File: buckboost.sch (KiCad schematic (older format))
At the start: 20 parts, among them SW1 SPST, U1 TPS63060

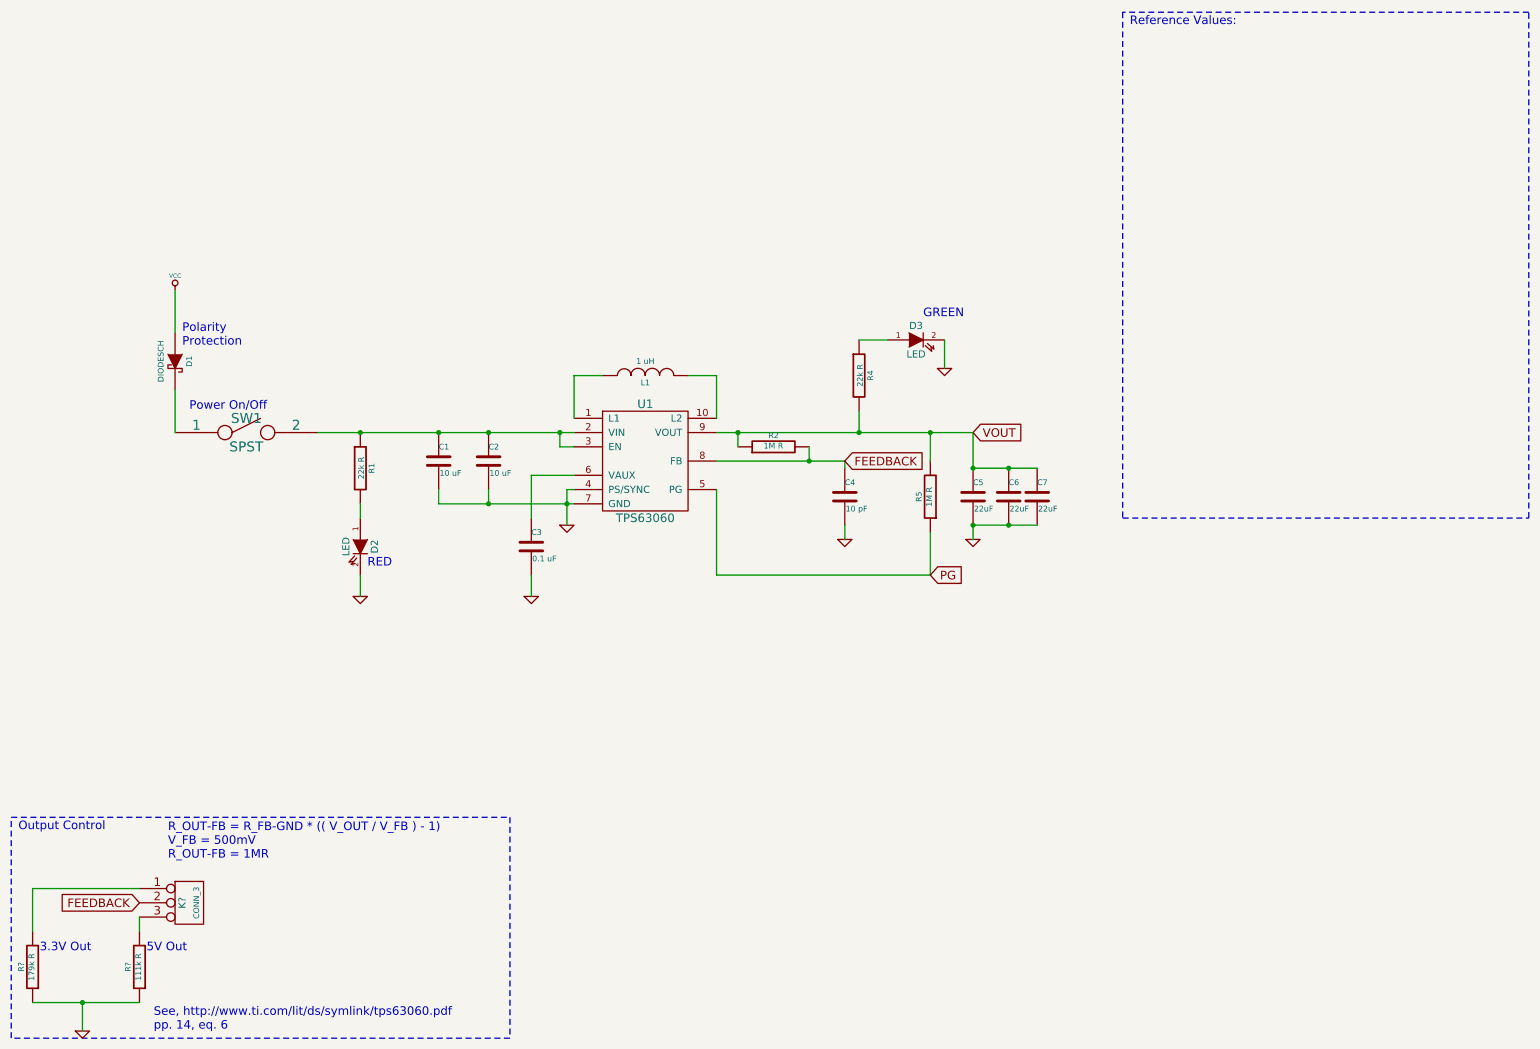
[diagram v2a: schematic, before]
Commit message: Added reference value chart from TI datasheet.
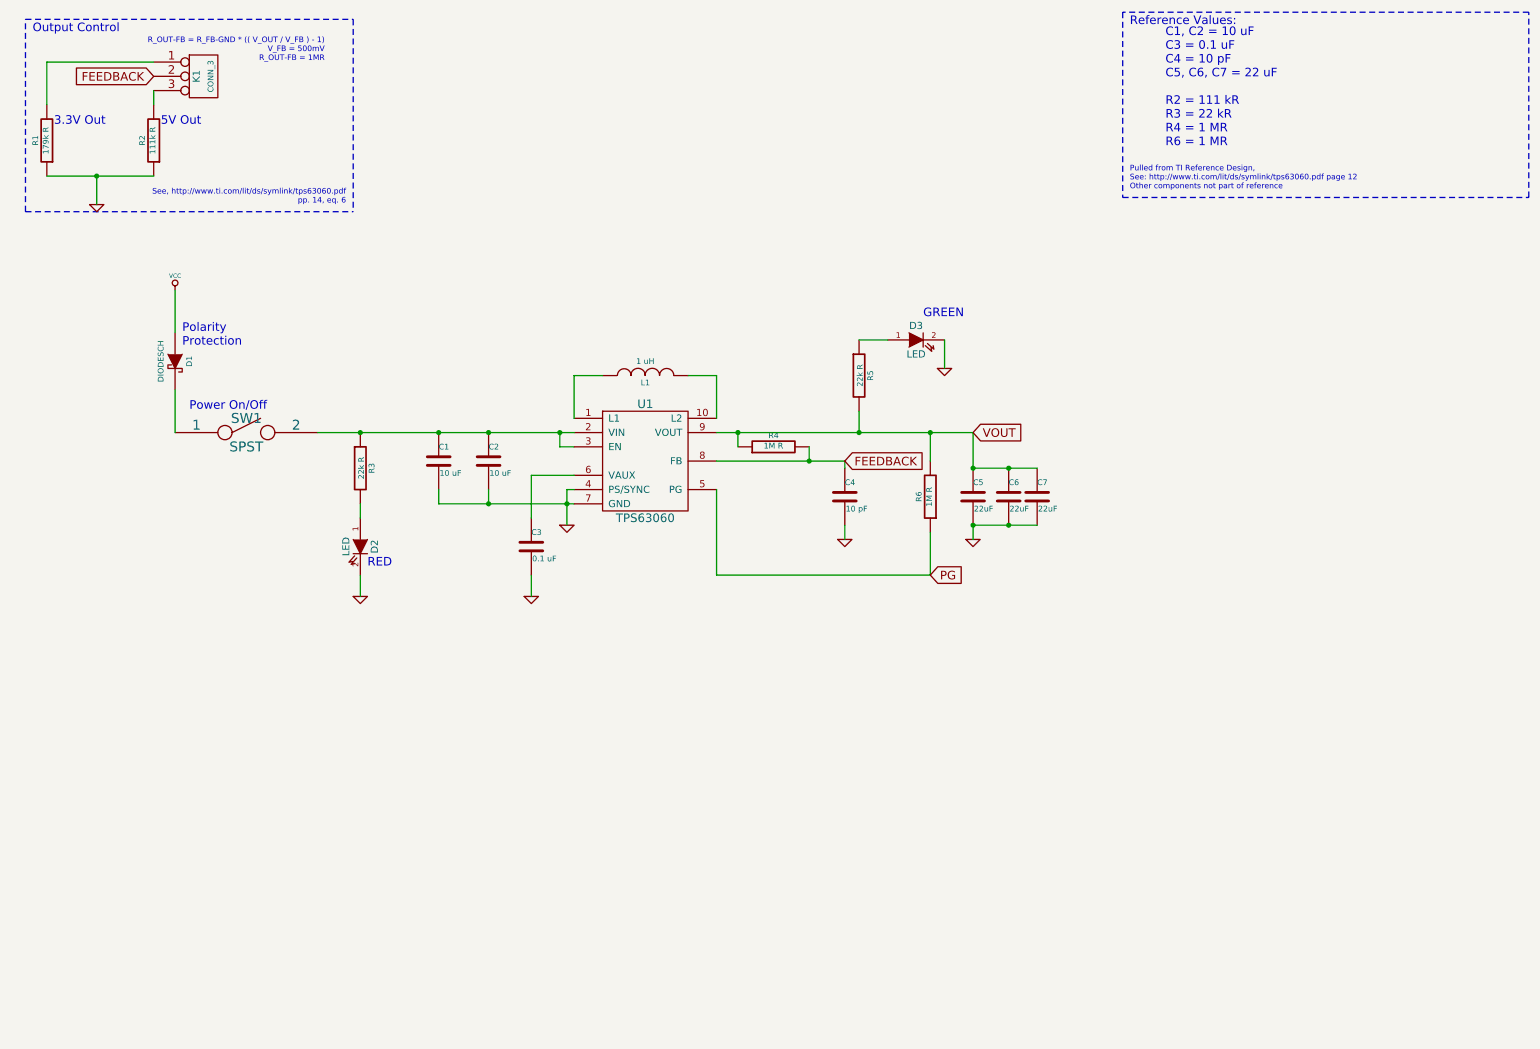
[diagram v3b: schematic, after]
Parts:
- gave numbers to parts that had none: 3
- renumbered R1 to R3, R2 to R4, R4 to R5, R5 to R6
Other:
- note added: "C1, C2 = 10 uF\nC3 = 0.1 uF\nC4 = 10 pF\nC5, C6, C7 = 22 uF\n\nR2 = 111 kR\nR3 = 22 kR\nR4 = 1 MR\nR6 = 1 MR\n"
- note added: "Pulled from TI Reference Design,\nSee: http://www.ti.com/lit/ds/symlink/tps63060.pdf page 12\nOther components not part of reference"
- moved on the sheet: K1, R1, R2
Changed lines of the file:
@@
 $EndComp
 $Comp
-L GND #PWR4
+L GND #PWR5
 U 1 1 56ED0689
 P 4400 4150
-F 0 "#PWR4" H 4400 4150 30  0001 C CNN
+F 0 "#PWR5" H 4400 4150 30  0001 C CNN
 F 1 "GND" H 4400 4080 30  0001 C CNN
 F 2 "" H 4400 4150 60  0000 C CNN
@@
 $EndComp
 $Comp
-L VCC #PWR1
+L VCC #PWR2
 U 1 1 56ED06A7
 P 1650 2500
-F 0 "#PWR1" H 1650 2600 30  0001 C CNN
+F 0 "#PWR2" H 1650 2600 30  0001 C CNN
 F 1 "VCC" H 1650 2600 30  0000 C CNN
 F 2 "" H 1650 2500 60  0000 C CNN
@@
 $EndComp
 $Comp
-L GND #PWR3
+L GND #PWR4
 U 1 1 56ED0918
 P 4150 4650
-F 0 "#PWR3" H 4150 4650 30  0001 C CNN
+F 0 "#PWR4" H 4150 4650 30  0001 C CNN
 F 1 "GND" H 4150 4580 30  0001 C CNN
 F 2 "" H 4150 4650 60  0000 C CNN
@@
 $EndComp
 $Comp
-L R R2
+L R R4
 U 1 1 56ED0C06
 P 5850 3600
-F 0 "R2" V 5930 3600 40  0000 C CNN
+F 0 "R4" V 5930 3600 40  0000 C CNN
 F 1 "1M R" V 5857 3601 40  0000 C CNN
 F 2 "" V 5780 3600 30  0000 C CNN
@@
 $EndComp
 $Comp
-L GND #PWR5
+L GND #PWR6
 U 1 1 56ED0DD5
 P 6350 4250
-F 0 "#PWR5" H 6350 4250 30  0001 C CNN
+F 0 "#PWR6" H 6350 4250 30  0001 C CNN
 F 1 "GND" H 6350 4180 30  0001 C CNN
 F 2 "" H 6350 4250 60  0000 C CNN
@@
 $EndComp
 $Comp
-L R R5
+L R R6
 U 1 1 56ED0E93
 P 6950 3950
-F 0 "R5" V 7030 3950 40  0000 C CNN
+F 0 "R6" V 7030 3950 40  0000 C CNN
 F 1 "1M R" V 6957 3951 40  0000 C CNN
 F 2 "" V 6880 3950 30  0000 C CNN
@@
 $EndComp
 $Comp
-L GND #PWR7
+L GND #PWR8
 U 1 1 56ED0F95
 P 7250 4250
-F 0 "#PWR7" H 7250 4250 30  0001 C CNN
+F 0 "#PWR8" H 7250 4250 30  0001 C CNN
 F 1 "GND" H 7250 4180 30  0001 C CNN
 F 2 "" H 7250 4250 60  0000 C CNN
@@
 Power On/Off
 $Comp
-L R R4
+L R R5
 U 1 1 56EE6E39
 P 6450 3100
-F 0 "R4" V 6530 3100 40  0000 C CNN
+F 0 "R5" V 6530 3100 40  0000 C CNN
 F 1 "22k R" V 6457 3101 40  0000 C CNN
 F 2 "" V 6380 3100 30  0000 C CNN
@@
 $EndComp
 $Comp
-L GND #PWR6
+L GND #PWR7
 U 1 1 56EE6F42
 P 7050 3050
-F 0 "#PWR6" H 7050 3050 30  0001 C CNN
+F 0 "#PWR7" H 7050 3050 30  0001 C CNN
 F 1 "GND" H 7050 2980 30  0001 C CNN
 F 2 "" H 7050 3050 60  0000 C CNN
@@
 $EndComp
 $Comp
-L R R1
+L R R3
 U 1 1 56EF9A6F
 P 2950 3750
-F 0 "R1" V 3030 3750 40  0000 C CNN
+F 0 "R3" V 3030 3750 40  0000 C CNN
 F 1 "22k R" V 2957 3751 40  0000 C CNN
 F 2 "" V 2880 3750 30  0000 C CNN
@@
 $EndComp
 $Comp
-L GND #PWR2
+L GND #PWR3
 U 1 1 56EF9C2C
 P 2950 4650
-F 0 "#PWR2" H 2950 4650 30  0001 C CNN
+F 0 "#PWR3" H 2950 4650 30  0001 C CNN
 F 1 "GND" H 2950 4580 30  0001 C CNN
 F 2 "" H 2950 4650 60  0000 C CNN
@@
 Wire Notes Line
 	11150 550  8300 550
-Wire Notes Line
-	8300 550  8300 4100
-Wire Notes Line
-	8300 4100 11150 4100
-Wire Notes Line
-	11150 4100 11150 550
-Text GLabel 1400 6800 0    60   Input ~ 0
+Text GLabel 1500 1000 0    60   Input ~ 0
 FEEDBACK
 $Comp
-L CONN_3 K?
+L CONN_3 K1
 U 1 1 56EFC39A
-P 1750 6800
-F 0 "K?" V 1700 6800 50  0000 C CNN
-F 1 "CONN_3" V 1800 6800 40  0000 C CNN
-F 2 "" H 1750 6800 60  0000 C CNN
-F 3 "" H 1750 6800 60  0000 C CNN
-	1    1750 6800
-	1    0    0    -1
-$EndComp
-$Comp
-L R R?
+P 1850 1000
+F 0 "K1" V 1800 1000 50  0000 C CNN
+F 1 "CONN_3" V 1900 1000 40  0000 C CNN
+F 2 "" H 1850 1000 60  0000 C CNN
+F 3 "" H 1850 1000 60  0000 C CNN
+	1    1850 1000
+	1    0    0    -1
+$EndComp
+$Comp
+L R R2
 U 1 1 56EFC5B1
-P 1400 7250
-F 0 "R?" V 1480 7250 40  0000 C CNN
-F 1 "111k R" V 1407 7251 40  0000 C CNN
-F 2 "" V 1330 7250 30  0000 C CNN
-F 3 "" H 1400 7250 30  0000 C CNN
-	1    1400 7250
+P 1500 1450
+F 0 "R2" V 1580 1450 40  0000 C CNN
+F 1 "111k R" V 1507 1451 40  0000 C CNN
+F 2 "" V 1430 1450 30  0000 C CNN
+F 3 "" H 1500 1450 30  0000 C CNN
+	1    1500 1450
 	-1   0    0    1
 $EndComp
 $Comp
-L R R?
+L R R1
 U 1 1 56EFC6E5
-P 650 7250
-F 0 "R?" V 730 7250 40  0000 C CNN
-F 1 "179k R" V 657 7251 40  0000 C CNN
-F 2 "" V 580 7250 30  0000 C CNN
-F 3 "" H 650 7250 30  0000 C CNN
-	1    650  7250
+P 750 1450
+F 0 "R1" V 830 1450 40  0000 C CNN
+F 1 "179k R" V 757 1451 40  0000 C CNN
+F 2 "" V 680 1450 30  0000 C CNN
+F 3 "" H 750 1450 30  0000 C CNN
+	1    750  1450
 	-1   0    0    1
 $EndComp
 Wire Wire Line
-	1400 6900 1400 7000
-Wire Wire Line
-	1400 6700 650  6700
-Wire Wire Line
-	650  6700 650  7000
-$Comp
-L GND #PWR?
+	1500 1100 1500 1200
+Wire Wire Line
+	1500 900  750  900
+Wire Wire Line
+	750  900  750  1200
+$Comp
+L GND #PWR1
 U 1 1 56EFC80B
-P 1000 7700
-F 0 "#PWR?" H 1000 7700 30  0001 C CNN
-F 1 "GND" H 1000 7630 30  0001 C CNN
-F 2 "" H 1000 7700 60  0000 C CNN
-F 3 "" H 1000 7700 60  0000 C CNN
-	1    1000 7700
-	1    0    0    -1
-$EndComp
-Wire Wire Line
-	650  7500 1400 7500
-Wire Wire Line
-	1000 7500 1000 7700
-Connection ~ 1000 7500
-Text Notes 1450 7150 0    60   ~ 0
+P 1100 1900
+F 0 "#PWR1" H 1100 1900 30  0001 C CNN
+F 1 "GND" H 1100 1830 30  0001 C CNN
+F 2 "" H 1100 1900 60  0000 C CNN
+F 3 "" H 1100 1900 60  0000 C CNN
+	1    1100 1900
+	1    0    0    -1
+$EndComp
+Wire Wire Line
+	750  1700 1500 1700
+Wire Wire Line
+	1100 1700 1100 1900
+Connection ~ 1100 1700
+Text Notes 1550 1350 0    60   ~ 0
 5V Out
-Text Notes 700  7150 0    60   ~ 0
+Text Notes 800  1350 0    60   ~ 0
 3.3V Out
-Wire Notes Line
-	500  6200 4000 6200
-Wire Notes Line
-	4000 6200 4000 7750
-Wire Notes Line
-	4000 7750 500  7750
-Wire Notes Line
-	500  7750 500  6200
-Text Notes 550  6300 0    60   ~ 0
+Text Notes 650  700  0    60   ~ 0
 Output Control
-Text Notes 1600 6500 0    60   ~ 0
+Text Notes 2700 900  2    39   ~ 0
 R_OUT-FB = R_FB-GND * (( V_OUT / V_FB ) - 1)\nV_FB = 500mV\nR_OUT-FB = 1MR
-Text Notes 1500 7700 0    60   ~ 0
+Text Notes 2850 1900 2    39   ~ 0
 See, http://www.ti.com/lit/ds/symlink/tps63060.pdf\npp. 14, eq. 6
+Text Notes 8350 1800 0    39   ~ 0
+Pulled from TI Reference Design,\nSee: http://www.ti.com/lit/ds/symlink/tps63060.pdf page 12\nOther components not part of reference
+Text Notes 8600 1500 0    60   ~ 0
+C1, C2 = 10 uF\nC3 = 0.1 uF\nC4 = 10 pF\nC5, C6, C7 = 22 uF\n\nR2 = 111 kR\nR3 = 22 kR\nR4 = 1 MR\nR6 = 1 MR\n
+Wire Notes Line
+	8300 1850 11150 1850
+Wire Notes Line
+	8300 550  8300 1850
+Wire Notes Line
+	11150 1850 11150 550
+Wire Notes Line
+	600  1950 2900 1950
+Wire Notes Line
+	600  1950 600  600
+Wire Notes Line
+	600  600  2900 600
+Wire Notes Line
+	2900 600  2900 1950
 $EndSCHEMATC
